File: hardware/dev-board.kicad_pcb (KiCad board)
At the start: 2 copper layers, 6 parts, among them J1 Debug, J2 USB_C_Receptacle_USB2.0, U1 E73-2G4M08S1C

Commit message: Dev Board v1.0.0.0
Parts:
- removed JP1: Jumper, Connector_PinHeader_2.54mm:PinHeader_1x02_P2.54mm_Vertical
- added J3: Conn_01x18_Male, Connector_PinHeader_2.54mm:PinHeader_1x18_P2.54mm_Vertical, B.Cu at (123.9, 88.5)
- added J4: Conn_01x18_Male, Connector_PinHeader_2.54mm:PinHeader_1x18_P2.54mm_Vertical, B.Cu at (123.9, 108.8)
- moved J2 15.4 mm to (164.1, 98.6), turned to 90 degrees
- moved R1 11.1 mm to (158.8, 96.8), turned to 180 degrees
- moved U1 7.91 mm to (131.8, 98.6), turned to 90 degrees
- moved R2 3.90 mm to (158.8, 99.8), turned to 180 degrees
- moved J1 1.73 mm to (150.0, 98.4), turned to 180 degrees
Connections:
- net Net-(J2-PadA6) renamed /D+
- net Net-(J2-PadA7) renamed /D-
- J2 pad A4: Net-(J2-PadA4) -> /VBUS
- J2 pad A9: Net-(J2-PadA4) -> /VBUS
- J2 pad B4: Net-(J2-PadA4) -> /VBUS
- J2 pad B9: Net-(J2-PadA4) -> /VBUS
- U1 pad 1: Net-(U1-Pad1) -> /P1.11
- U1 pad 10: Net-(U1-Pad10) -> /P0.30
- U1 pad 11: Net-(U1-Pad11) -> /P0.00
- U1 pad 12: Net-(U1-Pad12) -> /P0.26
- U1 pad 13: Net-(U1-Pad13) -> /P0.11
- U1 pad 14: Net-(U1-Pad14) -> /P0.06
- U1 pad 15: Net-(U1-Pad15) -> /P0.05
- U1 pad 16: Net-(U1-Pad16) -> /P0.08
- U1 pad 17: Net-(U1-Pad17) -> /P1.09
- U1 pad 18: Net-(U1-Pad18) -> /P0.04
- U1 pad 19: /VDD -> +3V3
- U1 pad 2: Net-(U1-Pad2) -> /P1.10
- U1 pad 20: Net-(U1-Pad20) -> /P0.12
- U1 pad 22: Net-(U1-Pad22) -> /P0.07
- U1 pad 23: /VDDH -> +3V3
- U1 pad 26: Net-(U1-Pad26) -> /P0.18
- U1 pad 28: Net-(U1-Pad28) -> /P0.15
- U1 pad 3: Net-(U1-Pad3) -> /P0.03
- U1 pad 30: Net-(U1-Pad30) -> /P0.17
- U1 pad 32: Net-(U1-Pad32) -> /P0.20
- U1 pad 33: Net-(U1-Pad33) -> /P0.13
- U1 pad 34: Net-(U1-Pad34) -> /P0.22
- U1 pad 35: Net-(U1-Pad35) -> /P0.24
- U1 pad 38: Net-(U1-Pad38) -> /P1.02
- U1 pad 4: Net-(U1-Pad4) -> /P0.28
- U1 pad 40: Net-(U1-Pad40) -> /P1.04
- U1 pad 41: Net-(U1-Pad41) -> /P0.09
- U1 pad 42: Net-(U1-Pad42) -> /P1.06
- U1 pad 43: Net-(U1-Pad43) -> /P0.10
- U1 pad 6: Net-(U1-Pad6) -> /P1.13
- U1 pad 7: Net-(U1-Pad7) -> /P0.02
- U1 pad 8: Net-(U1-Pad8) -> /P0.29
- U1 pad 9: Net-(U1-Pad9) -> /P0.31
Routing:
- net /VBUS: track 0.00 -> 46.3 mm, vias 0 -> 2
- net /P0.12: track 0.00 -> 35.3 mm, vias 0 -> 1
- net /D+: track 0.00 -> 34.3 mm
- net /D-: track 0.00 -> 33.2 mm
- net /P0.04: track 0.00 -> 32.2 mm, vias 0 -> 1
- net /SWO: track 0.00 -> 30.7 mm, vias 0 -> 2
- net /P0.08: track 0.00 -> 29.2 mm, vias 0 -> 1
- net /SWDCLK: track 0.00 -> 28.8 mm
- net /P0.07: track 0.00 -> 28.6 mm, vias 0 -> 1
- net /P0.15: track 0.00 -> 27.1 mm, vias 0 -> 1
- net /SWDIO: track 0.00 -> 26.4 mm
- net /P0.06: track 0.00 -> 26.1 mm, vias 0 -> 1
- net /P0.17: track 0.00 -> 25.8 mm, vias 0 -> 1
- net /P0.20: track 0.00 -> 25.0 mm, vias 0 -> 1
- net /P0.22: track 0.00 -> 23.9 mm, vias 0 -> 1
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- added copper zone on B.Cu, net +3V3
- added copper zone on F.Cu, net GND
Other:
- board outline added: 46 x 23.1 mm
- net class Default: clearance 0.2 -> 0.127; trace_width 0.25 -> 0.127; via_dia 0.8 -> 0.45; via_drill 0.4 -> 0.2
- rule trace_clearance: 0.2 -> 0.127
- rule trace_min: 0.2 -> 0.127
- rule via_min_drill: 0.3 -> 0.2
- rule via_min_size: 0.4 -> 0.45
- board text added: "Chameleon Electronics"
- board text added: "Dev Board"
- board text added: "v1.0.0"

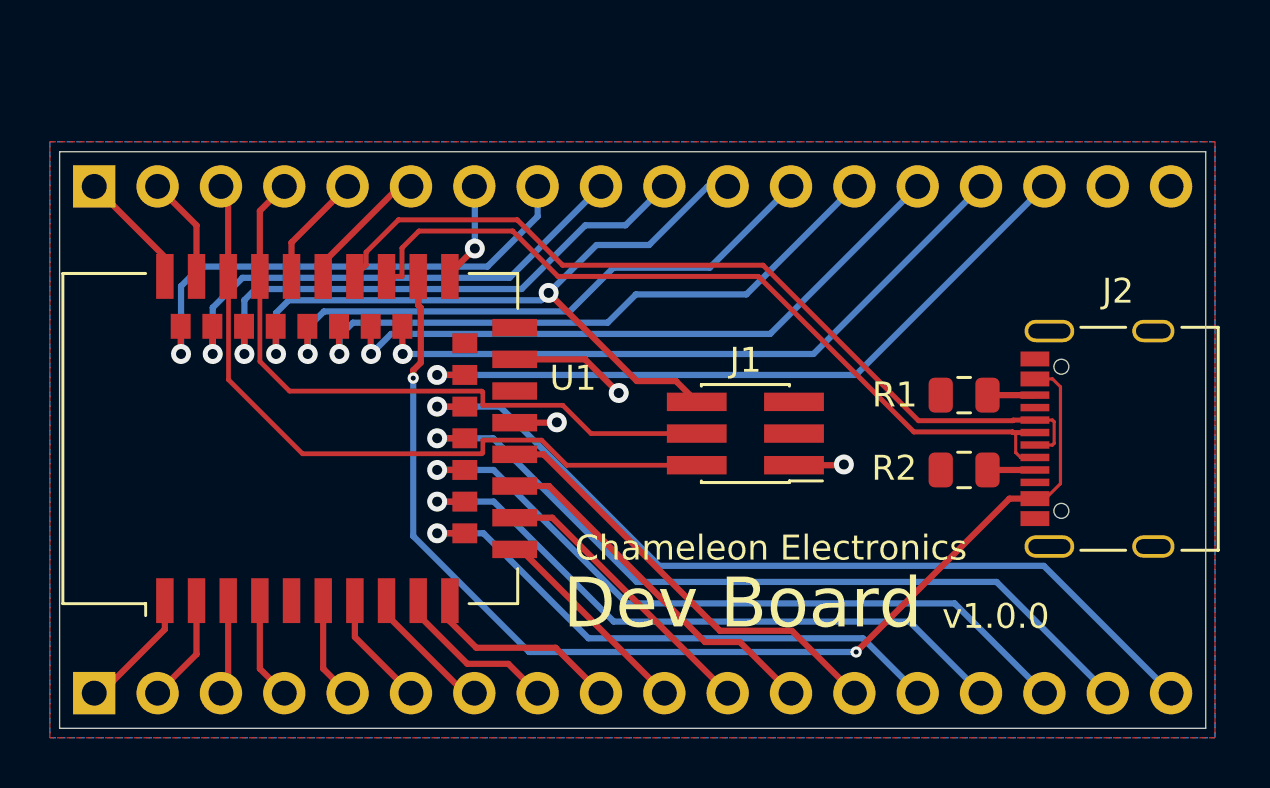
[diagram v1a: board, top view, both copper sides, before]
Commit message: Antenna keepout zone and rounded PCB corners
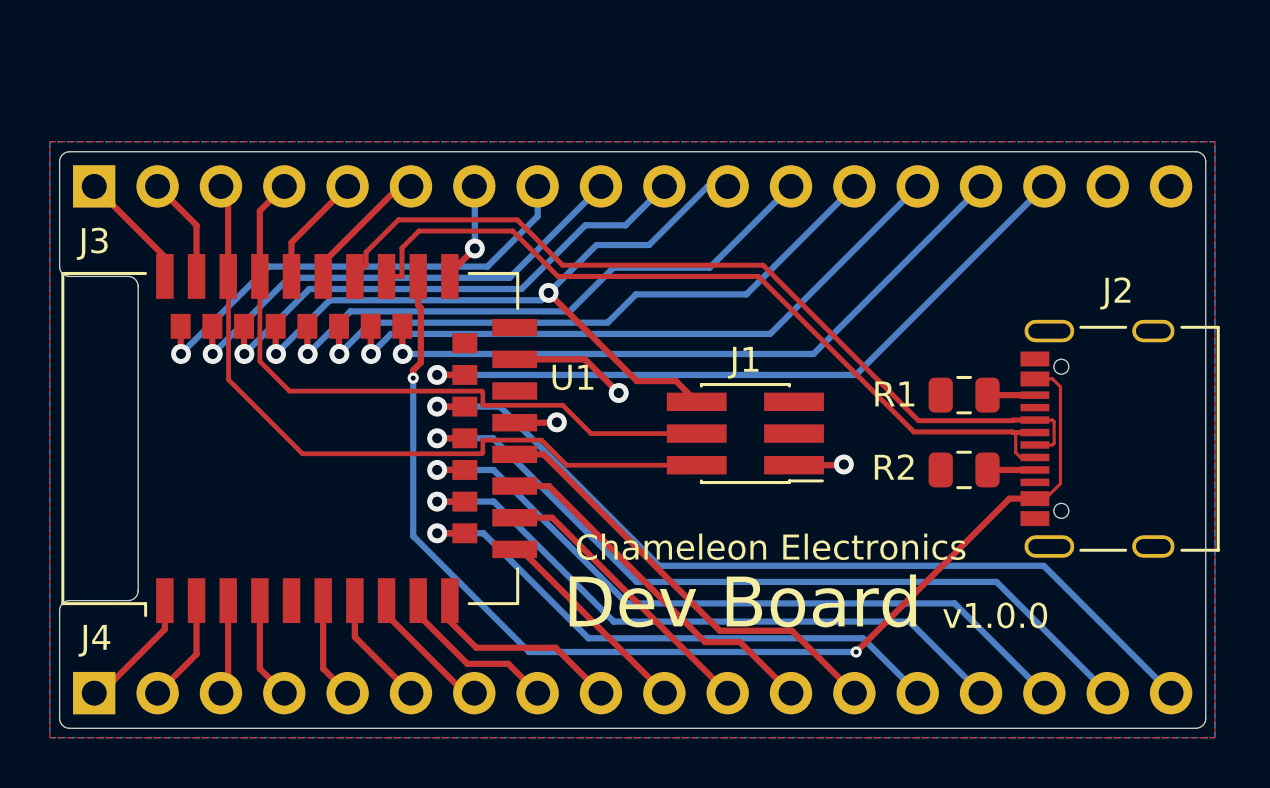
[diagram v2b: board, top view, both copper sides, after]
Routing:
- net /P1.06: track 20.5 -> 18.9 mm
- net /P1.02: track 22.0 -> 20.7 mm
- net /P1.04: track 20.6 -> 19.5 mm
- net /SWO: track 30.7 -> 29.8 mm
- net /P0.22: track 23.9 -> 23.3 mm
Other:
- outline, holes or cut-outs redrawn
- board text added: "0.00"
- board text added: "0.02"
- board text added: "0.04"
- board text added: "0.05"
- board text added: "0.06"
- board text added: "0.07"
- board text added: "0.08"
- board text added: "0.09"
- board text added: "0.10"
- board text added: "0.11"
- board text added: "0.12"
- board text added: "0.13"
- board text added: "0.15"
- board text added: "0.17"
- board text added: "0.18"
- board text added: "0.20"
- board text added: "0.22"
- board text added: "0.24"
- board text added: "0.26"
- board text added: "0.28"
- board text added: "0.29"
- board text added: "0.30"
- board text added: "0.31"
- board text added: "1.00"
- board text added: "1.02"
- board text added: "1.04"
- board text added: "1.06"
- board text added: "1.09"
- board text added: "1.10"
- board text added: "1.11"
- board text added: "1.13"
- board text added: "3V3"
- board text added: "GND"
- board text added: "SWCLK"
- board text added: "SWDIO"

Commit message: Use standard Debug connector (#2) and USB impendance matched (#3)
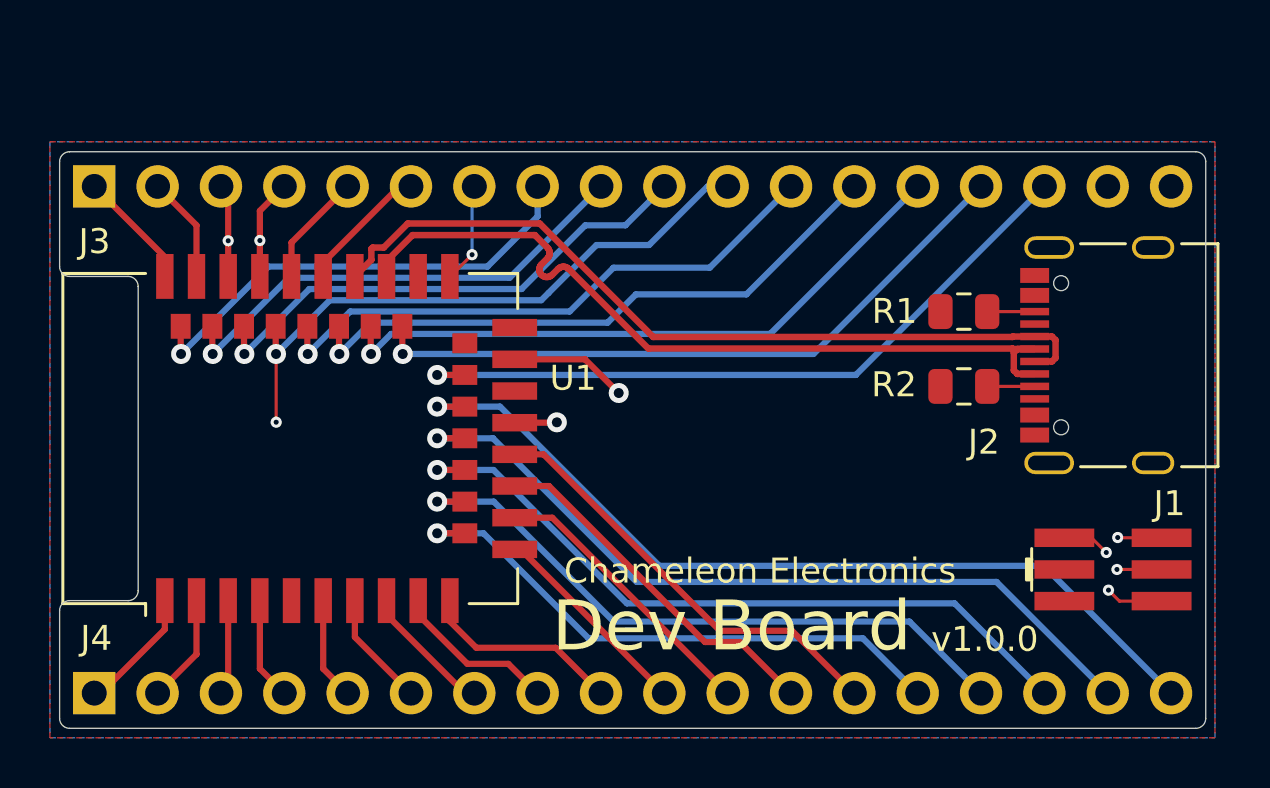
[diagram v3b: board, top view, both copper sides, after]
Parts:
- J1: value Debug -> Conn_Chameleon_SWD; footprint Connector_PinHeader_1.27mm:PinHeader_2x03_P1.27mm_Vertical_SMD -> IoT_Home:Chameleon_SWD_Header
- moved J1 15.7 mm to (164.7, 103.8), turned to 0 degrees
- moved J2 3.35 mm to (164.1, 95.2)
- moved R1 3.35 mm to (158.8, 93.5)
- moved R2 3.35 mm to (158.8, 96.5)
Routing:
- net /VBUS: track 46.3 -> 0.00 mm, vias 2 -> 0
- net /SWO: track 29.8 -> 63.2 mm, vias 2 -> 3
- net /SWDCLK: track 28.8 -> 51.7 mm, vias 0 -> 2
- net /SWDIO: track 26.4 -> 46.9 mm, vias 0 -> 2
- net /D+: track 34.3 -> 32.8 mm
- added copper zone on In1.Cu, net GND
- added copper zone on In2.Cu, net GND
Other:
- copper layers 2 -> 4
- net class USB added: clearance 0.127, trace_width 0.261112, via_dia 0.45, via_drill 0.2

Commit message: Release 1.0.0
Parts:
- removed J2: USB_C_Receptacle_USB2.0, Connector_USB:USB_C_Receptacle_Palconn_UTC16-G
- removed R1, R2: 5.1k, Resistor_SMD:R_0805_2012Metric
- moved J1 5.21 mm to (164.7, 98.6)
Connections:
- J1 pad 3: Net-(J1-Pad3) -> /P0.18
- U1 pad 25: /DCCH -> (no net)
- U1 pad 27: /VBUS -> (no net)
- U1 pad 29: /D- -> (no net)
- U1 pad 31: /D+ -> (no net)
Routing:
- net /D-: track 32.8 -> 0.00 mm
- net /D+: track 32.8 -> 0.00 mm
- net /P0.18: track 4.03 -> 31.3 mm, vias 1 -> 0
- net /SWO: track 63.2 -> 50.3 mm, vias 3 -> 2
- net /SWDCLK: track 51.7 -> 45.7 mm, vias 2 -> 1
- net /SWDIO: track 46.9 -> 44.5 mm, vias 2 -> 1
- net Net-(J2-PadB5): track 1.90 -> 0.00 mm
- net Net-(J2-PadA5): track 1.90 -> 0.00 mm
- removed copper zone on In1.Cu, net GND
- removed copper zone on In2.Cu, net GND
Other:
- copper layers 4 -> 2
- net class Default: clearance 0.127 -> 0.2; trace_width 0.127 -> 0.25; via_dia 0.45 -> 0.8; via_drill 0.2 -> 0.4
- net class USB removed
- rule trace_clearance: 0.127 -> 0.2
- board text added: "nRF52840"
- board text removed: "Chameleon Electronics"

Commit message: Fix Silkcreen Pin
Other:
- board text added: "0.03"

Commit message: Update render and silkcreen version number
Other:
- board text added: "v1.0.1"
- board text removed: "v1.0.0"
